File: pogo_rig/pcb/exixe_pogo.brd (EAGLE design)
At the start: 100 x 80 mm, 14 parts, among them X1 USB-MICROB

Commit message: working on pogo rig
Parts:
- added C1, C2, R1: (no value), clock:0805
- added C3, C4: (no value), clock:C1210
- added IC1: REG1117, clock:SOT223
- added IC2: STM32F030F4, stm32f030f4:TSSOP20
- added JP3, JP4: (no value), clock:1X04/90
- added LED1, LED2: (no value), clock:CHIP-LED0805
- added S1, S2: TAC_SWITCHSMD, clock:TACTILE-SWITCH-SMD
- added U$11, U$12, U$13, U$14: M3_MOUNTING_HOLE, clock:M3_MOUNTING_HOLE_PACK
- moved X1 81.9 mm to (45.0, 1.54), turned to 0 degrees
- moved JP2 27.0 mm to (45.0, 38.0)
- moved JP1 25.6 mm to (45.0, 33.0)
- moved U$10 24.0 mm to (73.0, 8.50)
- moved U$8 23.5 mm to (73.0, 55.5)
- moved N1 20.0 mm to (45.0, 50.0)
- moved U$1 9.57 mm to (63.0, 12.0)
- moved U$4 8.18 mm to (3.50, 22.0)
- moved U$5 8.03 mm to (30.5, 22.0)
- moved U$6 2.45 mm to (30.5, 42.0)
- moved U$7 2.21 mm to (17.0, 55.5)
- moved U$9 2.21 mm to (17.0, 8.50)
- moved U$2 1.94 mm to (7.00, 12.0)
- moved U$3 1.58 mm to (3.50, 42.0)
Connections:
- new net +3V3: C1.1, C2.1, C3.1, IC1.2, IC1.4, IC2.16, IC2.5, JP3.2, JP4.2, LED1.A, U$1.3V, U$2.3V
- new net +5V: C4.1, IC1.3, X1.VBUS
- new net CS: IC2.10, U$1.CS, U$2.CS
- new net EXIXE_RST: U$1.RST, U$2.RST
- new net GND: C1.2, C2.2, C3.2, C4.2, IC1.1, IC2.1, IC2.15, JP3.1, JP4.1, R1.2, U$1.GND, U$2.GND, X1.GND, X1.P1, X1.P2, X1.P3, X1.P4, X1.P5, X1.P6
- new net MISO: IC2.12, U$1.MISO, U$2.MISO
- new net MOSI: IC2.13, U$1.MOSI, U$2.MOSI
- new net N$1: N1.1, U$1.DIGIT_1, U$2.DIGIT_1
- new net N$10: N1.9, U$1.DIGIT_9, U$2.DIGIT_9
- new net N$11: N1.0, U$1.DIGIT_0, U$2.DIGIT_0
- new net N$12: N1.RHDP, U$2.DOT_RIGHT
- new net N$13: N1.LHDP, U$1.DOT_LEFT, U$2.DOT_LEFT
- new net N$14: N1.A, U$1.ANODE, U$2.ANODE
- new net N$15: LED1.C, R1.1
- new net N$2: IC2.4, S1.3
- new net N$3: N1.2, U$1.DIGIT_2, U$2.DIGIT_2
- new net N$4: N1.3, U$1.DIGIT_3, U$2.DIGIT_3
- new net N$5: N1.4, U$1.DIGIT_4, U$2.DIGIT_4
- new net N$6: N1.5, U$1.DIGIT_5, U$2.DIGIT_5
- new net N$7: N1.6, U$1.DIGIT_6, U$2.DIGIT_6
- new net N$8: N1.7, U$1.DIGIT_7, U$2.DIGIT_7
- new net N$9: N1.8, U$1.DIGIT_8, U$2.DIGIT_8
- new net RX: IC2.9
- new net SCK: IC2.11, U$1.SCK, U$2.SCK
- new net SWCLK: IC2.20
- new net SWDIO: IC2.19
- new net TX: IC2.8
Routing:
- net +3V3: track 0.00 -> 10.8 mm, vias 0 -> 3
- net +5V: track 0.00 -> 8.83 mm
- net N$15: track 0.00 -> 2.60 mm
- added copper zone on layer 16, net +3V3
- added copper zone on layer 1, net GND
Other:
- board size 100 x 80 mm -> 90 x 60 mm

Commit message: working on pogo board
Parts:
- added R2, R3: (no value), clock:0805
- added U$15, U$16, U$17, U$18: M3_MOUNTING_HOLE, clock:M3_MOUNTING_HOLE_PACK
- moved LED1 3.81 mm to (32.0, 28.2), turned to 0 degrees
- moved LED2 3.81 mm to (57.8, 28.2), turned to 0 degrees
- moved R1 3.81 mm to (29.5, 28.2), turned to 270 degrees
- moved U$13 0.90 mm to (85.6, 42.0)
- moved U$14 0.90 mm to (85.6, 22.0)
- moved U$10 0.90 mm to (73.0, 9.40)
- moved U$3 0.90 mm to (4.40, 42.0)
- moved U$4 0.90 mm to (4.40, 22.0)
- moved U$9 0.90 mm to (17.0, 9.40)
- moved U$11 0.90 mm to (60.4, 42.0)
- moved U$12 0.90 mm to (60.4, 22.0)
- moved U$5 0.90 mm to (29.6, 22.0)
- moved U$6 0.90 mm to (29.6, 42.0)
- moved U$7 0.90 mm to (17.0, 54.6)
- moved U$8 0.90 mm to (73.0, 54.6)
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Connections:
- new net +180V: JP1.HV, JP2.HV, U$1.HV, U$2.HV
- new net EXIXE_SWCLK: JP3.3, U$1.CLK, U$2.CLK
- new net EXIXE_SWDIO: JP3.4, U$1.DIO, U$2.DIO
- new net HV_EN: IC2.18, JP1.EN, JP2.EN, R3.1
- new net N$16: IC2.6, LED1.A
- new net N$18: LED2.C, R2.1
- new net N$19: IC2.17, LED2.A
- new net USER_BUTTON: IC2.14, S2.1
- net +3V3: no longer JP4.2, LED1.A
- net +5V: now also JP1.5V, JP2.5V, R3.2
- net EXIXE_RST: now also IC2.7
- net GND: now also JP1.GND, JP1.GND2, JP2.GND, JP2.GND2, R2.2, S1.1, S1.2, S2.3; no longer JP4.1
- net RX: now also JP4.2
- net SWCLK: now also JP4.3
- net SWDIO: now also JP4.4
- net TX: now also JP4.1
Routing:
- net +180V: track 0.00 -> 99.5 mm
- net CS: track 0.00 -> 84.2 mm, vias 0 -> 1
- net N$14: track 0.00 -> 78.6 mm
- net EXIXE_SWCLK: track 0.00 -> 76.1 mm
- net N$13: track 0.00 -> 70.7 mm
- net MISO: track 0.00 -> 70.7 mm, vias 0 -> 1
- net EXIXE_RST: track 0.00 -> 70.4 mm, vias 0 -> 1
- net N$8: track 0.00 -> 70.3 mm
- net N$7: track 0.00 -> 69.7 mm
- net N$11: track 0.00 -> 69.4 mm
- net N$5: track 0.00 -> 69.1 mm
- net N$4: track 0.00 -> 69.1 mm
- net N$1: track 0.00 -> 69.0 mm
- net N$9: track 0.00 -> 68.7 mm
- net N$6: track 0.00 -> 68.3 mm
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
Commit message: pogo rig mostly finished
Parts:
- added JP5: (no value), pinhead:1X02
- added JP6, JP7: (no value), pinhead:1X06
- added LED3: (no value), clock:CHIP-LED0805
- added R4, R5: (no value), clock:0805
- added TP1, TP10, TP11, TP2, TP3, TP4, TP5, TP6, TP7, TP8, TP9: TEST-POINT3X5, clock:PAD.03X.05
- JP3, JP4: device clock:1X04/90 -> pinhead:1X04
- moved JP3 3.81 mm to (30.0, 9.81)
- moved JP4 3.81 mm to (60.0, 9.81)
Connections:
- new net N$17: JP5.1, R4.1
- new net N$20: IC2.2, TP1.P$1
- new net N$21: IC2.3, TP2.P$1
- new net N$22: TP4.P$1, U$1.PF1
- new net N$23: TP5.P$1, U$1.PB6
- new net N$24: TP6.P$1, U$1.PA9
- new net N$25: TP7.P$1, U$1.PA1
- new net N$26: TP8.P$1, U$2.PF0
- new net N$27: TP9.P$1, U$2.PF1
- new net N$28: TP10.P$1, U$2.PB3
- new net N$29: TP11.P$1, U$2.PB6
- new net N$30: TP3.P$1, U$1.PF0
- new net N$31: LED3.C, R5.1
- net +180V: now also R4.2
- net +3V3: now also JP6.1, JP7.1, LED3.A
- net GND: now also JP5.2, JP6.6, JP7.6, R5.2
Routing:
- net N$22: track 0.00 -> 5.72 mm
- net N$23: track 0.00 -> 5.34 mm
- net N$24: track 0.00 -> 5.22 mm
- net N$30: track 0.00 -> 5.10 mm
- net N$25: track 0.00 -> 4.85 mm
- net N$7: track 69.7 -> 65.4 mm
- net N$8: track 70.3 -> 66.5 mm
- net N$17: track 0.00 -> 3.60 mm
- net N$26: track 0.00 -> 3.42 mm
- net N$27: track 0.00 -> 3.39 mm
- net N$13: track 70.7 -> 67.4 mm
- net N$28: track 0.00 -> 3.21 mm
- net N$29: track 0.00 -> 3.00 mm
- net +180V: track 99.5 -> 102.4 mm
- net +3V3: track 17.4 -> 20.1 mm, vias 4 -> 5
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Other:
- board text added: "3V3"
- board text added: "A"
- board text added: "B"
- board text added: "C"
- board text added: "D"
- board text added: "E"
- board text added: "EXCLK"
- board text added: "EXDIO"
- board text added: "F"
- board text added: "G"
- board text added: "GND"
- board text added: "H"
- board text added: "HV"
- board text added: "HV_ON"
- board text added: "PA9"
- board text added: "PB1"
- board text added: "PF0"
- board text added: "PF1"
- board text added: "PGCLK"
- board text added: "PGDIO"
- board text added: "PGRX"
- board text added: "PGTX"
- board text added: "PWR"
- board text added: "RST"
- board text added: "exixe pogo rig dekuNukem 2017"

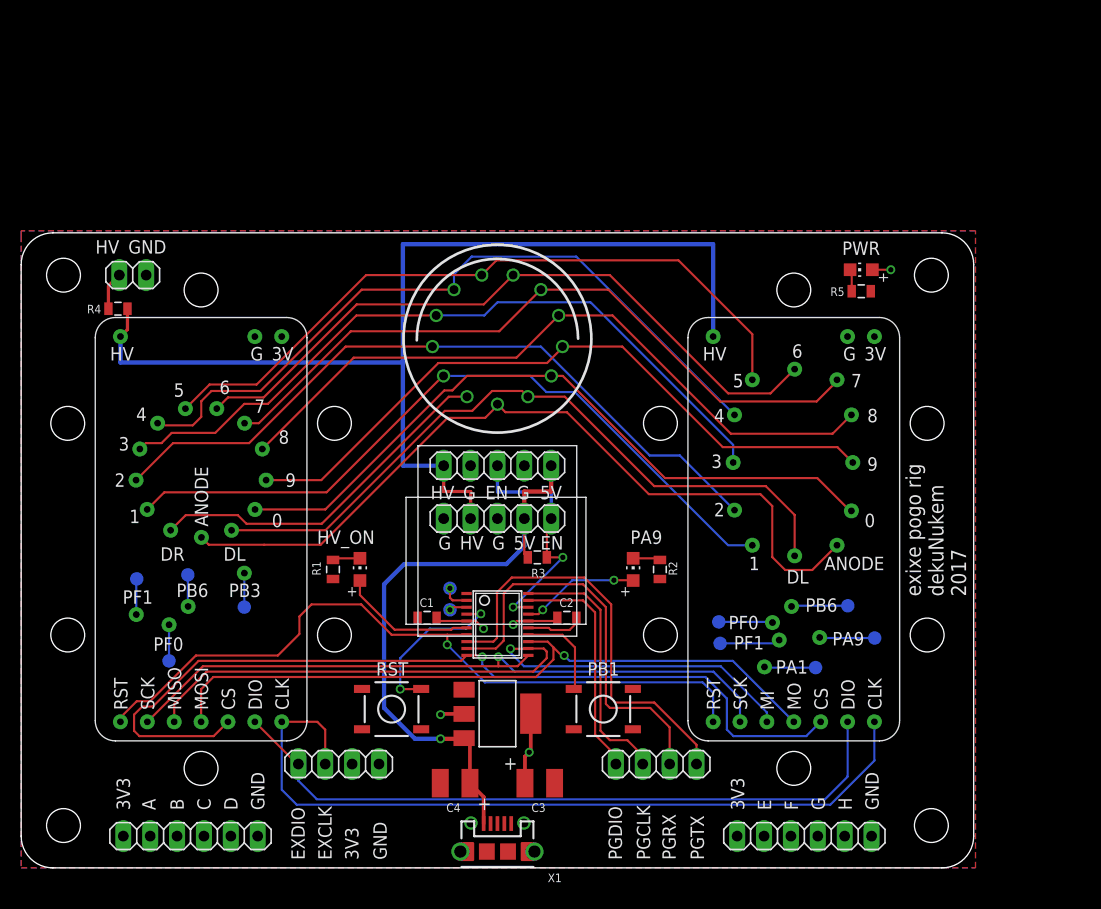
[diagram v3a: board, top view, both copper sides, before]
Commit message: changed pogo pad size
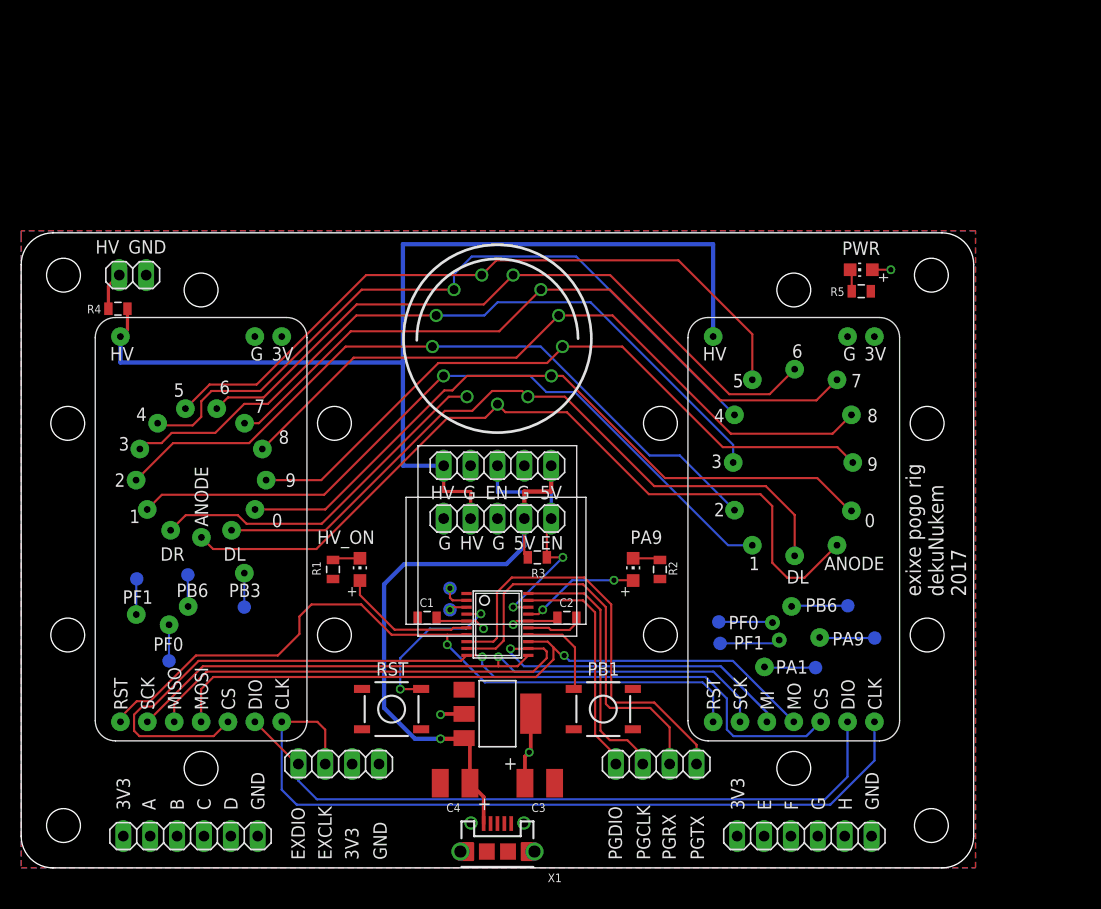
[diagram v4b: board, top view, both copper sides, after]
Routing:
- net N$14: track 76.2 -> 77.5 mm
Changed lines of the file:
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@@
 <setting verticaltext="up"/>
 </settings>
-<grid distance="5" unitdist="mil" unit="mil" style="lines" multiple="1" display="no" altdistance="2" altunitdist="mil" altunit="mil"/>
+<grid distance="1" unitdist="mil" unit="mil" style="lines" multiple="1" display="no" altdistance="2" altunitdist="mil" altunit="mil"/>
 <layers>
 <layer number="1" name="Top" color="4" fill="1" visible="yes" active="yes"/>
@@
 <contactref element="N1" pad="1"/>
 <contactref element="U$2" pad="DIGIT_1"/>
-<wire x1="11.9058" y1="33.8647" x2="13.5249" y2="35.4838" width="0.2032" layer="1"/>
-<wire x1="13.5249" y1="35.4838" x2="28.8551" y2="35.4838" width="0.2032" layer="1"/>
-<wire x1="28.8551" y1="35.4838" x2="39.855" y2="46.4837" width="0.2032" layer="1"/>
 <wire x1="39.855" y1="46.4837" x2="39.9058" y2="46.4837" width="0.2032" layer="1"/>
 <wire x1="48.1076" y1="46.482" x2="39.9075" y2="46.482" width="0.2032" layer="16"/>
@@
 <wire x1="49.6316" y1="44.958" x2="48.1076" y2="46.482" width="0.2032" layer="16"/>
 <wire x1="66.7995" y1="30.4825" x2="52.324" y2="44.958" width="0.2032" layer="16"/>
+<wire x1="11.9058" y1="33.8647" x2="13.2963" y2="35.2552" width="0.2032" layer="1"/>
+<wire x1="13.2963" y1="35.2552" x2="28.6265" y2="35.2552" width="0.2032" layer="1"/>
+<wire x1="28.6265" y1="35.2552" x2="39.855" y2="46.4837" width="0.2032" layer="1"/>
 </signal>
 <signal name="N$3">
@@
 <wire x1="31.6992" y1="53.2384" x2="43.7096" y2="53.2384" width="0.2032" layer="1"/>
 <wire x1="43.7096" y1="53.2384" x2="46.4813" y2="56.0101" width="0.2032" layer="1"/>
-<wire x1="46.4813" y1="56.0101" x2="55.6229" y2="56.0101" width="0.2032" layer="1"/>
-<wire x1="55.6229" y1="56.0101" x2="66.802" y2="44.831" width="0.2032" layer="1"/>
-<wire x1="66.802" y1="44.831" x2="70.796" y2="44.831" width="0.2032" layer="1"/>
-<wire x1="70.796" y1="44.831" x2="73.0825" y2="47.1175" width="0.2032" layer="1"/>
+<wire x1="73.0825" y1="47.1175" x2="70.7198" y2="44.7548" width="0.2032" layer="1"/>
+<wire x1="70.7198" y1="44.7548" x2="66.9036" y2="44.7548" width="0.2032" layer="1"/>
+<wire x1="66.9036" y1="44.7548" x2="55.6483" y2="56.0101" width="0.2032" layer="1"/>
+<wire x1="55.6483" y1="56.0101" x2="46.4813" y2="56.0101" width="0.2032" layer="1"/>
 </signal>
 <signal name="N$8">
@@
 <wire x1="31.1404" y1="50.6984" x2="45.1699" y2="50.6984" width="0.2032" layer="1"/>
 <wire x1="45.1699" y1="50.6984" x2="49.1047" y2="54.6332" width="0.2032" layer="1"/>
-<wire x1="66.04" y1="44.069" x2="75.161" y2="44.069" width="0.2032" layer="1"/>
-<wire x1="66.04" y1="44.069" x2="55.4758" y2="54.6332" width="0.2032" layer="1"/>
-<wire x1="55.4758" y1="54.6332" x2="49.1047" y2="54.6332" width="0.2032" layer="1"/>
-<wire x1="75.161" y1="44.069" x2="77.0825" y2="45.9905" width="0.2032" layer="1"/>
-<wire x1="77.0825" y1="45.9905" x2="77.0825" y2="46.1175" width="0.2032" layer="1"/>
+<wire x1="77.0825" y1="46.1175" x2="75.1356" y2="44.1706" width="0.2032" layer="1"/>
+<wire x1="75.1356" y1="44.1706" x2="66.0908" y2="44.1706" width="0.2032" layer="1"/>
+<wire x1="66.0908" y1="44.1706" x2="55.6282" y2="54.6332" width="0.2032" layer="1"/>
+<wire x1="55.6282" y1="54.6332" x2="49.1047" y2="54.6332" width="0.2032" layer="1"/>
 </signal>
 <signal name="N$9">
@@
 <contactref element="N1" pad="A"/>
 <contactref element="U$2" pad="ANODE"/>
-<wire x1="17.033" y1="31.2241" x2="17.7263" y2="30.5308" width="0.2032" layer="1"/>
-<wire x1="17.7263" y1="30.5308" x2="22.9616" y2="30.5308" width="0.2032" layer="1"/>
 <wire x1="40.2844" y1="42.5196" x2="43.8404" y2="42.5196" width="0.2032" layer="1"/>
 <wire x1="43.8404" y1="42.5196" x2="45" y2="43.6792" width="0.2032" layer="1"/>
 <wire x1="45" y1="43.6792" x2="45" y2="43.8101" width="0.2032" layer="1"/>
-<wire x1="77.0825" y1="30.4825" x2="74.7432" y2="28.1432" width="0.2032" layer="1"/>
-<wire x1="74.7432" y1="28.1432" x2="72.1868" y2="28.1432" width="0.2032" layer="1"/>
-<wire x1="72.1868" y1="28.1432" x2="70.9676" y2="29.3624" width="0.2032" layer="1"/>
-<wire x1="70.9676" y1="29.3624" x2="70.9676" y2="34.1884" width="0.2032" layer="1"/>
 <wire x1="70.9676" y1="34.1884" x2="69.85" y2="35.306" width="0.2032" layer="1"/>
 <wire x1="59.309" y1="35.306" x2="51.562" y2="43.053" width="0.2032" layer="1"/>
@@
 <wire x1="45.7571" y1="43.053" x2="45" y2="43.8101" width="0.2032" layer="1"/>
 <wire x1="69.85" y1="35.306" x2="59.309" y2="35.306" width="0.2032" layer="1"/>
-<wire x1="22.9616" y1="30.5308" x2="28.2956" y2="30.5308" width="0.2032" layer="1"/>
-<wire x1="28.2956" y1="30.5308" x2="40.2844" y2="42.5196" width="0.2032" layer="1"/>
+<wire x1="77.0825" y1="30.4825" x2="74.0066" y2="27.4066" width="0.2032" layer="1"/>
+<wire x1="74.0066" y1="27.4066" x2="72.39" y2="27.4066" width="0.2032" layer="1"/>
+<wire x1="72.39" y1="27.4066" x2="70.9676" y2="28.829" width="0.2032" layer="1"/>
+<wire x1="70.9676" y1="28.829" x2="70.9676" y2="34.1884" width="0.2032" layer="1"/>
+<wire x1="17.033" y1="31.2241" x2="18.1327" y2="30.1244" width="0.2032" layer="1"/>
+<wire x1="18.1327" y1="30.1244" x2="27.8892" y2="30.1244" width="0.2032" layer="1"/>
+<wire x1="27.8892" y1="30.1244" x2="40.2844" y2="42.5196" width="0.2032" layer="1"/>
 </signal>
 <signal name="N$12">
